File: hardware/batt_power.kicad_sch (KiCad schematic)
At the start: 10 parts, among them J5 Conn_01x03, J6 Battery JST, Q1 Q_NMOS_GSD, U6 TPS7A2030PDBV

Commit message: Updated values to be in standard series
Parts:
- R5, R6: value 50k -> 22k
- R8: value 50k -> 51k
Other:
- note added: "Same as IREF resistor on radio, use tight tolerance resistors"
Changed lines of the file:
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@@
+		)
+	)
+	(text "Same as IREF resistor on radio,\nuse tight tolerance resistors"
+		(exclude_from_sim no)
+		(at 136.652 124.46 0)
+		(effects
+			(font
+				(size 0.762 0.762)
+			)
+			(justify left)
 		)
 	)
@@
 			)
 		)
-		(property "Value" "50k"
+		(property "Value" "22k"
 			(at 134.62 132.0799 0)
 			(effects
@@
 			)
 		)
-		(property "Value" "50k"
+		(property "Value" "22k"
 			(at 134.62 119.3799 0)
 			(effects
@@
 			)
 		)
-		(property "Value" "50k"
+		(property "Value" "51k"
 			(at 119.38 149.8599 0)
 			(effects

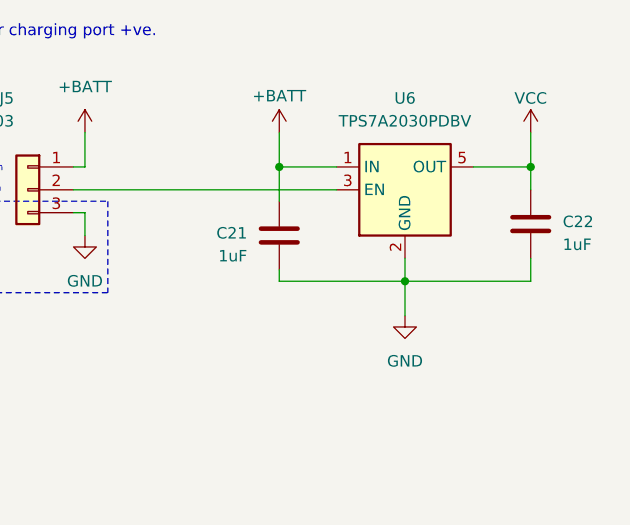
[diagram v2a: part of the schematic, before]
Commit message: Updated decoupling caps
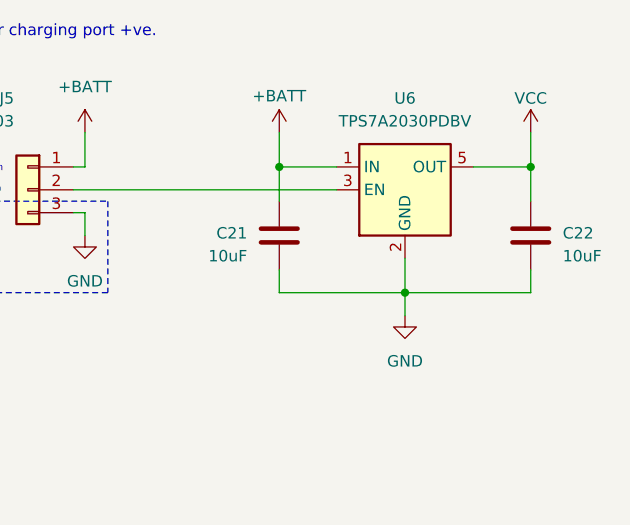
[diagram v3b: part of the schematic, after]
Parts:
- C21, C22: value 1uF -> 10uF
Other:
- moved on the sheet: C22
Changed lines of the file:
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@@
-	)
-	(junction
-		(at 177.8 68.58)
-		(diameter 0)
-		(color 0 0 0 0)
 	)
 	(junction
@@
 	)
 	(junction
+		(at 177.8 69.85)
+		(diameter 0)
+		(color 0 0 0 0)
+	)
+	(junction
 		(at 132.08 154.94)
 		(diameter 0)
@@
 	(wire
 		(pts
-			(xy 177.8 68.58) (xy 191.77 68.58)
-		)
-		(stroke
-			(width 0)
-			(type default)
-		)
-	)
-	(wire
-		(pts
-			(xy 177.8 72.39) (xy 177.8 68.58)
-		)
-		(stroke
-			(width 0)
-			(type default)
-		)
-	)
-	(wire
-		(pts
-			(xy 163.83 67.31) (xy 163.83 68.58)
-		)
-		(stroke
-			(width 0)
-			(type default)
-		)
-	)
-	(wire
-		(pts
-			(xy 191.77 55.88) (xy 191.77 58.42)
+			(xy 177.8 69.85) (xy 191.77 69.85)
+		)
+		(stroke
+			(width 0)
+			(type default)
+		)
+	)
+	(wire
+		(pts
+			(xy 177.8 72.39) (xy 177.8 69.85)
+		)
+		(stroke
+			(width 0)
+			(type default)
+		)
+	)
+	(wire
+		(pts
+			(xy 163.83 67.31) (xy 163.83 69.85)
+		)
+		(stroke
+			(width 0)
+			(type default)
+		)
+	)
+	(wire
+		(pts
+			(xy 191.77 55.88) (xy 191.77 59.69)
 		)
 		(stroke
@@
 	(wire
 		(pts
-			(xy 163.83 68.58) (xy 177.8 68.58)
+			(xy 163.83 69.85) (xy 177.8 69.85)
 		)
 		(stroke
@@
 	(wire
 		(pts
-			(xy 191.77 66.04) (xy 191.77 68.58)
+			(xy 191.77 67.31) (xy 191.77 69.85)
+		)
+		(stroke
+			(width 0)
+			(type default)
+		)
+	)
+	(wire
+		(pts
+			(xy 177.8 66.04) (xy 177.8 69.85)
 		)
 		(stroke
@@
 		(pts
 			(xy 132.08 154.94) (xy 132.08 157.48)
-		)
-		(stroke
-			(width 0)
-			(type default)
-		)
-	)
-	(wire
-		(pts
-			(xy 177.8 68.58) (xy 177.8 66.04)
 		)
 		(stroke
@@
 	(symbol
 		(lib_id "Device:C")
-		(at 191.77 62.23 0)
+		(at 191.77 63.5 0)
 		(unit 1)
 		(exclude_from_sim no)
@@
 		(dnp no)
 		(property "Reference" "C22"
-			(at 195.326 61.976 0)
+			(at 195.326 63.246 0)
 			(effects
 				(font
@@
 			)
 		)
-		(property "Value" "1uF"
-			(at 195.326 64.516 0)
+		(property "Value" "10uF"
+			(at 195.326 65.786 0)
 			(effects
 				(font
@@
 		)
 		(property "Footprint" ""
-			(at 192.7352 66.04 0)
+			(at 192.7352 67.31 0)
 			(effects
 				(font
@@
 		)
 		(property "Datasheet" "~"
-			(at 191.77 62.23 0)
+			(at 191.77 63.5 0)
 			(effects
 				(font
@@
 		)
 		(property "Description" "Unpolarized capacitor"
-			(at 191.77 62.23 0)
+			(at 191.77 63.5 0)
 			(effects
 				(font
@@
 			)
 		)
-		(property "Value" "1uF"
+		(property "Value" "10uF"
 			(at 160.274 65.786 0)
 			(effects

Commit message: Updated footprints for the IC's
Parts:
- U6: footprint Package_TO_SOT_SMD:SOT-23-5 -> Package_TO_SOT_SMD:SOT-23-5_HandSoldering
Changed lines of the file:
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@@
 			)
 		)
-		(property "Footprint" "Package_TO_SOT_SMD:SOT-23-5"
+		(property "Footprint" "Package_TO_SOT_SMD:SOT-23-5_HandSoldering"
 			(at 177.8 49.53 0)
 			(effects

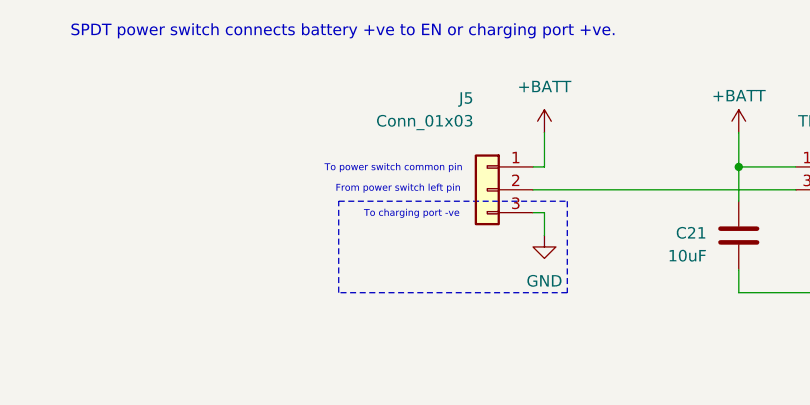
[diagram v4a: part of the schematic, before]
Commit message: Assigned footprints for connectors
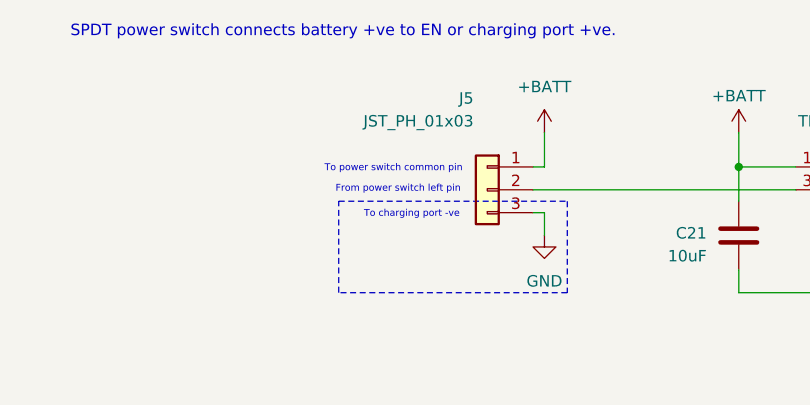
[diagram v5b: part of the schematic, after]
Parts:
- J5: value Conn_01x03 -> JST_PH_01x03; footprint (none) -> Connector_JST:JST_PH_B3B-PH-K_1x03_P2.00mm_Vertical
- J6: footprint (none) -> Connector_Wire:SolderWire-1sqmm_1x02_P7.8mm_D1.4mm_OD3.9mm
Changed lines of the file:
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@@
 			)
 		)
-		(property "Value" "Conn_01x03"
+		(property "Value" "JST_PH_01x03"
 			(at 134.366 50.8 0)
 			(effects
@@
 			)
 		)
-		(property "Footprint" ""
+		(property "Footprint" "Connector_JST:JST_PH_B3B-PH-K_1x03_P2.00mm_Vertical"
 			(at 135.89 58.42 0)
 			(effects
@@
 			)
 		)
-		(property "Footprint" ""
+		(property "Footprint" "Connector_Wire:SolderWire-1sqmm_1x02_P7.8mm_D1.4mm_OD3.9mm"
 			(at 54.61 80.01 0)
 			(effects

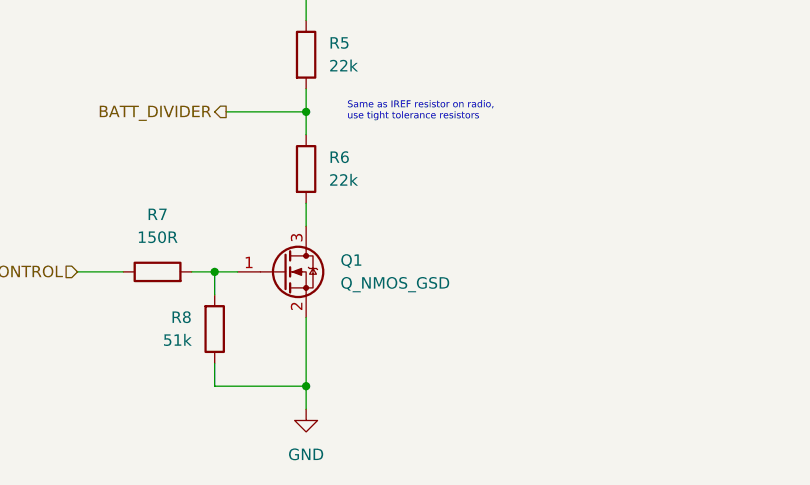
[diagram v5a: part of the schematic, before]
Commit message: Assigned footprint for mosfet
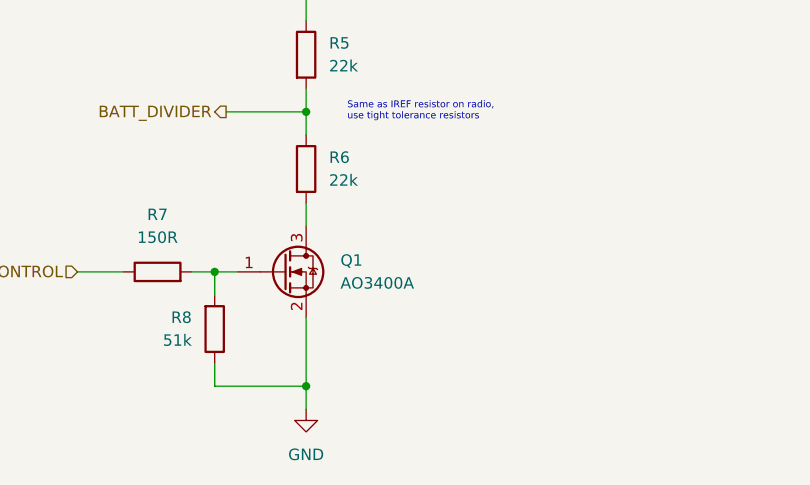
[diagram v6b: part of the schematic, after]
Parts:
- removed Q1: Q_NMOS_GSD, symbol Device:Q_NMOS_GSD
- added Q1: AO3400A, Package_TO_SOT_SMD:SOT-23, symbol Transistor_FET:AO3400A
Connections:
- net GND: now also Q1.2 (S)
- net at R6.2: now also Q1.3 (D)
- net at R7.2, R8.2: now also Q1.1 (G)
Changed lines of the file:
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@@
+	)
+	(symbol
+		(lib_id "Transistor_FET:AO3400A")
+		(at 129.54 142.24 0)
+		(unit 1)
+		(exclude_from_sim no)
+		(in_bom yes)
+		(on_board yes)
+		(dnp no)
+		(fields_autoplaced yes)
+		(property "Reference" "Q1"
+			(at 135.89 140.9699 0)
+			(effects
+				(font
+					(size 1.27 1.27)
+				)
+				(justify left)
+			)
+		)
+		(property "Value" "AO3400A"
+			(at 135.89 143.5099 0)
+			(effects
+				(font
+					(size 1.27 1.27)
+				)
+				(justify left)
+			)
+		)
+		(property "Footprint" "Package_TO_SOT_SMD:SOT-23"
+			(at 134.62 144.145 0)
+			(effects
+				(font
+					(size 1.27 1.27)
+					(italic yes)
+				)
+				(justify left)
+				(hide yes)
+			)
+		)
+		(property "Datasheet" "http://www.aosmd.com/pdfs/datasheet/AO3400A.pdf"
+			(at 134.62 146.05 0)
+			(effects
+				(font
+					(size 1.27 1.27)
+				)
+				(justify left)
+				(hide yes)
+			)
+		)
+		(property "Description" "30V Vds, 5.7A Id, N-Channel MOSFET, SOT-23"
+			(at 129.54 142.24 0)
+			(effects
+				(font
+					(size 1.27 1.27)
+				)
+				(hide yes)
+			)
+		)
+		(pin "2"
+		)
+		(pin "1"
+		)
+		(pin "3"
+		)
+		(instances
+			(project ""
+				(path "/c384ea46-0dfb-4673-b2f4-1f88fafbcaa5/f8f87cfe-571f-4a92-acee-79776e4ce004"
+					(reference "Q1")
+					(unit 1)
+				)
+			)
+		)
 	)
 	(symbol
@@
 					(unit 1)
 				)
-			)
-		)
-	)
-	(symbol
-		(lib_id "Device:Q_NMOS_GSD")
-		(at 129.54 142.24 0)
-		(unit 1)
-		(exclude_from_sim no)
-		(in_bom yes)
-		(on_board yes)
-		(dnp no)
-		(fields_autoplaced yes)
-		(property "Reference" "Q1"
-			(at 135.89 140.9699 0)
-			(effects
-				(font
-					(size 1.27 1.27)
-				)
-				(justify left)
-			)
-		)
-		(property "Value" "Q_NMOS_GSD"
-			(at 135.89 143.5099 0)
-			(effects
-				(font
-					(size 1.27 1.27)
-				)
-				(justify left)
-			)
-		)
-		(property "Footprint" ""
-			(at 134.62 139.7 0)
-			(effects
-				(font
-					(size 1.27 1.27)
-				)
-				(hide yes)
-			)
-		)
-		(property "Datasheet" "~"
-			(at 129.54 142.24 0)
-			(effects
-				(font
-					(size 1.27 1.27)
-				)
-				(hide yes)
-			)
-		)
-		(property "Description" "N-MOSFET transistor, gate/source/drain"
-			(at 129.54 142.24 0)
-			(effects
-				(font
-					(size 1.27 1.27)
-				)
-				(hide yes)
-			)
-		)
-		(pin "3"
-		)
-		(pin "2"
-		)
-		(pin "1"
-		)
-		(instances
-			(project ""
-				(path "/c384ea46-0dfb-4673-b2f4-1f88fafbcaa5/f8f87cfe-571f-4a92-acee-79776e4ce004"
-					(reference "Q1")
-					(unit 1)
-				)

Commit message: Assigned footprints for capacitors and inductors
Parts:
- C21, C22: footprint (none) -> Capacitor_SMD:C_0603_1608Metric_Pad1.08x0.95mm_HandSolder
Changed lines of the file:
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@@
 			)
 		)
-		(property "Footprint" ""
+		(property "Footprint" "Capacitor_SMD:C_0603_1608Metric_Pad1.08x0.95mm_HandSolder"
 			(at 192.7352 67.31 0)
 			(effects
@@
 			)
 		)
-		(property "Footprint" ""
+		(property "Footprint" "Capacitor_SMD:C_0603_1608Metric_Pad1.08x0.95mm_HandSolder"
 			(at 162.8648 67.31 0)
 			(effects

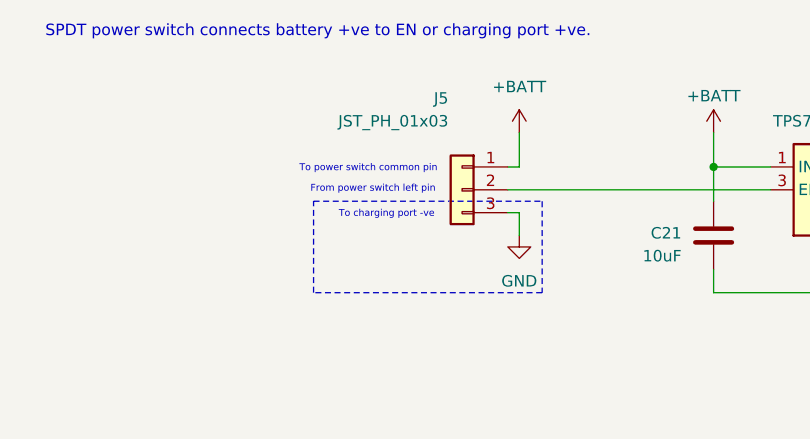
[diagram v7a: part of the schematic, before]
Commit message: Corrected pin order on JST connectors
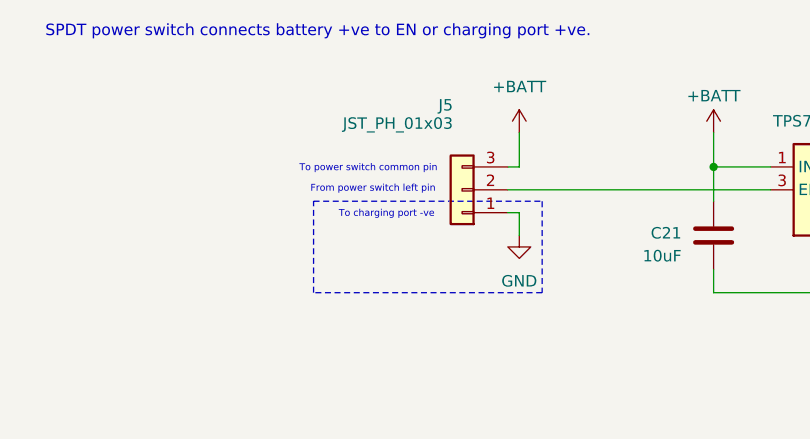
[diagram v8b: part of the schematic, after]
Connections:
- net +BATT: now also J5.3 (Pin_3); no longer J5.1 (Pin_1)
- net GND: now also J5.1 (Pin_1); no longer J5.3 (Pin_3)
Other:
- moved on the sheet: J5
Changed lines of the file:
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@@
 	(symbol
 		(lib_id "Connector_Generic:Conn_01x03")
-		(at 135.89 58.42 0)
-		(mirror y)
+		(at 135.89 58.42 180)
 		(unit 1)
 		(exclude_from_sim no)
@@
 		(dnp no)
 		(property "Reference" "J5"
-			(at 134.366 48.26 0)
+			(at 134.874 49.022 0)
 			(effects
 				(font
@@
 		)
 		(property "Value" "JST_PH_01x03"
-			(at 134.366 50.8 0)
+			(at 134.874 51.054 0)
 			(effects
 				(font
